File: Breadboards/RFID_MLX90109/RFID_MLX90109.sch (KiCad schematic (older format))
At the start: 24 parts, among them P101 CONN_01X08, Q101 Q_NMOS_GSD, U101 MLX90109

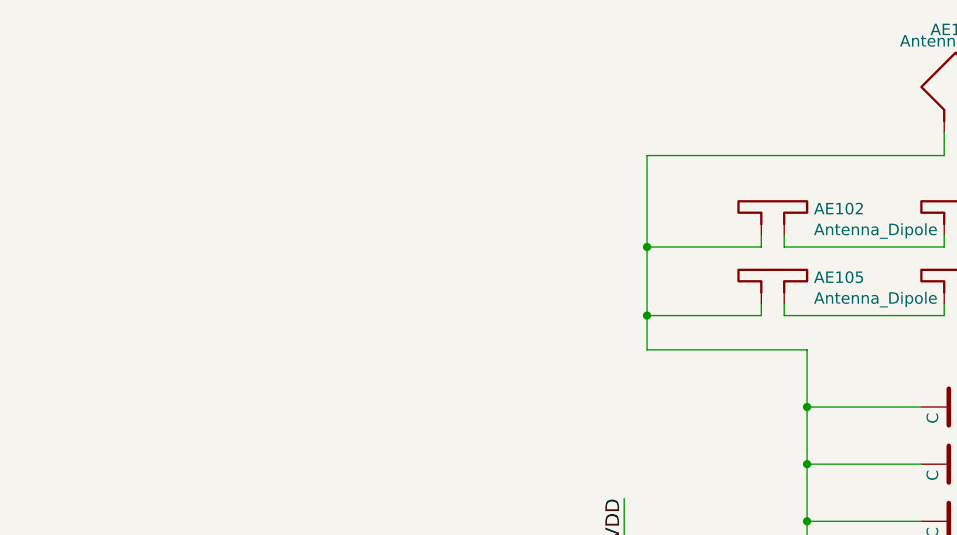
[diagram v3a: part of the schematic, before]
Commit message: Adds 2 Antennas for 125kHz antenna (Back and Front)
- Antenna is connected via 2 jumpers
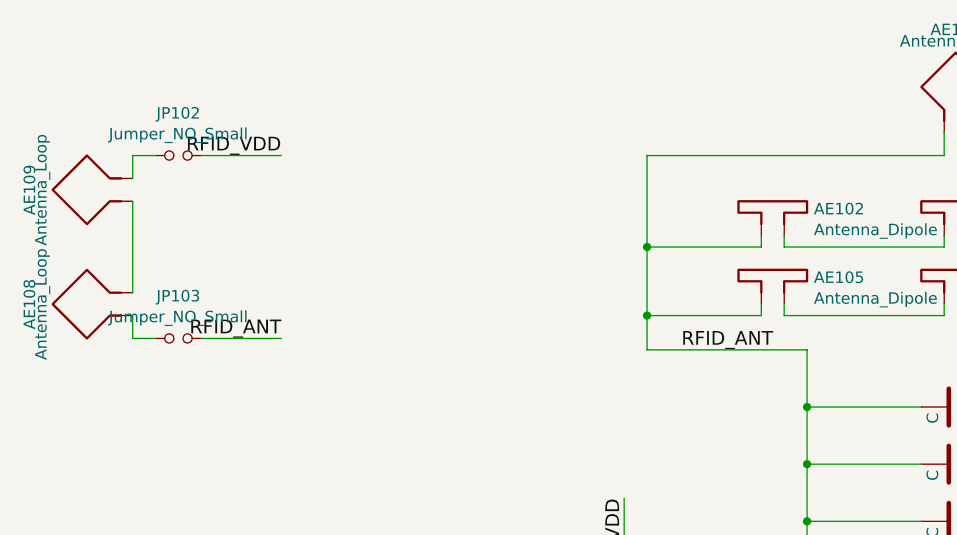
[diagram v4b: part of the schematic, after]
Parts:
- added AE108, AE109: Antenna_Loop, Octanis3:125kHz_PCB_Antenna, symbol Antenna_Loop
- added JP102, JP103: Jumper_NO_Small, Pin_Headers:Pin_Header_Straight_1x02_Pitch2.54mm, symbol Jumper_NO_Small
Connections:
- net labels added: RFID_ANT
- wire segments 75 -> 82
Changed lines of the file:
@@
 	1    0    0    -1
 $EndComp
-Wire Wire Line
-	5850 3200 6950 3200
-Wire Wire Line
-	5800 3650 7550 3650
-Wire Wire Line
-	5800 3800 7550 3800
-Wire Wire Line
-	4200 3650 4800 3650
-Wire Wire Line
-	4250 3950 4800 3950
-Connection ~ 4500 3950
-Wire Wire Line
-	3250 3950 3950 3950
-Wire Wire Line
-	3700 3800 4800 3800
-Wire Wire Line
-	4600 3500 4800 3500
-Wire Wire Line
-	4600 3050 5100 3050
-Wire Wire Line
-	5850 3050 5400 3050
-Wire Wire Line
-	5850 2050 5850 3500
-Connection ~ 5850 3200
-Connection ~ 4600 3050
-Connection ~ 5850 3050
-Wire Wire Line
-	4500 3950 4500 4400
-Wire Wire Line
-	3950 4200 3800 4200
-Wire Wire Line
-	3800 4200 3800 3950
-Connection ~ 3800 3950
-Wire Wire Line
-	4500 4200 4250 4200
-Connection ~ 4500 4200
-Connection ~ 4300 3650
-Connection ~ 4700 3950
-Wire Wire Line
-	4500 4700 4500 4800
-Wire Wire Line
-	4600 2800 5100 2800
-Connection ~ 4600 2800
-Connection ~ 4600 2550
-Wire Wire Line
-	4600 2050 4600 3500
-Wire Wire Line
-	4600 2550 5100 2550
-Wire Wire Line
-	5400 2550 5850 2550
-Connection ~ 5850 2550
-Wire Wire Line
-	5400 2800 5850 2800
-Connection ~ 5850 2800
-Wire Wire Line
-	4600 2300 5100 2300
-Connection ~ 4600 2300
-Wire Wire Line
-	5400 2300 5850 2300
-Connection ~ 5850 2300
-Wire Wire Line
-	8950 2550 8950 3050
-Wire Wire Line
-	3800 3100 3800 2700
-Wire Wire Line
-	3800 3400 3800 3800
-Connection ~ 3800 3800
-Wire Wire Line
-	3400 3800 3350 3800
-Wire Wire Line
-	5800 3950 6100 3950
-Wire Wire Line
-	6000 3950 6000 4250
-Connection ~ 6000 3950
-Wire Wire Line
-	6400 3950 6900 3950
-Wire Wire Line
-	4500 5200 4500 5300
-Wire Wire Line
-	4100 5000 4200 5000
-Wire Wire Line
-	5850 3500 5800 3500
-Wire Wire Line
-	6650 3600 6650 3800
-Connection ~ 6650 3800
-Wire Wire Line
-	6650 3200 6650 3300
-Connection ~ 6650 3200
-Wire Wire Line
-	6950 3600 6950 3650
-Connection ~ 6950 3650
-Wire Wire Line
-	6950 3200 6950 3300
-Wire Wire Line
-	5300 1550 5300 1600
-Wire Wire Line
-	5300 1600 6000 1600
-Wire Wire Line
-	6000 1600 6000 1550
-Wire Wire Line
-	4500 1850 4500 1900
-Wire Wire Line
-	4500 1900 5200 1900
-Wire Wire Line
-	5200 1900 5200 1850
-Wire Wire Line
-	5300 1850 5300 1900
-Wire Wire Line
-	5300 1900 6000 1900
-Wire Wire Line
-	6000 1900 6000 1850
-Wire Wire Line
-	4500 1550 4500 1600
-Wire Wire Line
-	4500 1600 5200 1600
-Wire Wire Line
-	5200 1600 5200 1550
-Wire Wire Line
-	3900 1200 3900 2050
-Wire Wire Line
-	3900 2050 4600 2050
-Wire Wire Line
-	5200 1100 5200 1200
-Wire Wire Line
-	5200 1200 3900 1200
-Wire Wire Line
-	5300 1100 5300 1200
-Wire Wire Line
-	5300 1200 6850 1200
-Wire Wire Line
-	6850 1200 6850 2050
-Wire Wire Line
-	6850 2050 5850 2050
-Wire Wire Line
-	6100 1550 6100 1600
-Wire Wire Line
-	6100 1600 6850 1600
-Connection ~ 6850 1600
-Wire Wire Line
-	6100 1850 6100 1900
-Wire Wire Line
-	6100 1900 6850 1900
-Connection ~ 6850 1900
-Wire Wire Line
-	4400 1550 4400 1600
-Wire Wire Line
-	4400 1600 3900 1600
-Connection ~ 3900 1600
-Wire Wire Line
-	4400 1850 4400 1900
-Wire Wire Line
-	4400 1900 3900 1900
-Connection ~ 3900 1900
-Wire Wire Line
-	3800 3500 3250 3500
-Connection ~ 3800 3500
 Text Label 3250 3500 0    60   ~ 0
 RFID_SPEED
@@
 Text Label 7100 3800 0    60   ~ 0
 RFID_CLOCK
-Wire Wire Line
-	6000 4150 6900 4150
-Connection ~ 6000 4150
 Text Label 6450 4150 0    60   ~ 0
 RFID_MODE
-Wire Wire Line
-	10350 3500 9700 3500
-Wire Wire Line
-	10350 3600 9700 3600
-Wire Wire Line
-	10350 3700 9700 3700
-Wire Wire Line
-	10350 3800 9700 3800
-Wire Wire Line
-	10350 3900 9700 3900
-Wire Wire Line
-	10350 4000 9700 4000
 Text Label 9700 3800 0    60   ~ 0
 RFID_CLOCK
@@
 	1    0    0    -1
 $EndComp
-Wire Wire Line
-	10350 4100 9700 4100
-Wire Wire Line
-	10350 4200 9700 4200
 Text Label 9700 4100 0    60   ~ 0
 RFID_SPEED
@@
 	1    0    0    -1
 $EndComp
+$Comp
+L Antenna_Loop AE108
+U 1 1 5A1309D1
+P 1450 1900
+F 0 "AE108" H 1500 2150 50  0000 C CNN
+F 1 "Antenna_Loop" H 1500 2100 50  0000 C CNN
+F 2 "Octanis3:125kHz_PCB_Antenna" H 1450 1900 50  0001 C CNN
+F 3 "" H 1450 1900 50  0001 C CNN
+	1    1450 1900
+	0    -1   -1   0
+$EndComp
+$Comp
+L Antenna_Loop AE109
+U 1 1 5A130BD8
+P 1450 1300
+F 0 "AE109" H 1500 1550 50  0000 C CNN
+F 1 "Antenna_Loop" H 1500 1500 50  0000 C CNN
+F 2 "Octanis3:125kHz_PCB_Antenna" H 1450 1300 50  0001 C CNN
+F 3 "" H 1450 1300 50  0001 C CNN
+	1    1450 1300
+	0    -1   1    0
+$EndComp
+$Comp
+L Jumper_NO_Small JP102
+U 1 1 5A130D13
+P 1850 1200
+F 0 "JP102" H 1850 1385 50  0000 C CNN
+F 1 "Jumper_NO_Small" H 1850 1294 50  0000 C CNN
+F 2 "Pin_Headers:Pin_Header_Straight_1x02_Pitch2.54mm" H 1850 1200 50  0001 C CNN
+F 3 "" H 1850 1200 50  0000 C CNN
+	1    1850 1200
+	1    0    0    -1
+$EndComp
+$Comp
+L Jumper_NO_Small JP103
+U 1 1 5A131038
+P 1850 2000
+F 0 "JP103" H 1850 2185 50  0000 C CNN
+F 1 "Jumper_NO_Small" H 1850 2094 50  0000 C CNN
+F 2 "Pin_Headers:Pin_Header_Straight_1x02_Pitch2.54mm" H 1850 2000 50  0001 C CNN
+F 3 "" H 1850 2000 50  0000 C CNN
+	1    1850 2000
+	1    0    0    -1
+$EndComp
+Wire Wire Line
+	5850 3200 6950 3200
+Wire Wire Line
+	5800 3650 7550 3650
+Wire Wire Line
+	5800 3800 7550 3800
+Wire Wire Line
+	4200 3650 4800 3650
+Wire Wire Line
+	4250 3950 4800 3950
+Connection ~ 4500 3950
+Wire Wire Line
+	3250 3950 3950 3950
+Wire Wire Line
+	3700 3800 4800 3800
+Wire Wire Line
+	4600 3500 4800 3500
+Wire Wire Line
+	4600 3050 5100 3050
+Wire Wire Line
+	5850 3050 5400 3050
+Wire Wire Line
+	5850 2050 5850 3500
+Connection ~ 5850 3200
+Connection ~ 4600 3050
+Connection ~ 5850 3050
+Wire Wire Line
+	4500 3950 4500 4400
+Wire Wire Line
+	3950 4200 3800 4200
+Wire Wire Line
+	3800 4200 3800 3950
+Connection ~ 3800 3950
+Wire Wire Line
+	4500 4200 4250 4200
+Connection ~ 4500 4200
+Connection ~ 4300 3650
+Connection ~ 4700 3950
+Wire Wire Line
+	4500 4700 4500 4800
+Wire Wire Line
+	4600 2800 5100 2800
+Connection ~ 4600 2800
+Connection ~ 4600 2550
+Wire Wire Line
+	4600 2050 4600 3500
+Wire Wire Line
+	4600 2550 5100 2550
+Wire Wire Line
+	5400 2550 5850 2550
+Connection ~ 5850 2550
+Wire Wire Line
+	5400 2800 5850 2800
+Connection ~ 5850 2800
+Wire Wire Line
+	4600 2300 5100 2300
+Connection ~ 4600 2300
+Wire Wire Line
+	5400 2300 5850 2300
+Connection ~ 5850 2300
+Wire Wire Line
+	8950 2550 8950 3050
+Wire Wire Line
+	3800 3100 3800 2700
+Wire Wire Line
+	3800 3400 3800 3800
+Connection ~ 3800 3800
+Wire Wire Line
+	3400 3800 3350 3800
+Wire Wire Line
+	5800 3950 6100 3950
+Wire Wire Line
+	6000 3950 6000 4250
+Connection ~ 6000 3950
+Wire Wire Line
+	6400 3950 6900 3950
+Wire Wire Line
+	4500 5200 4500 5300
+Wire Wire Line
+	4100 5000 4200 5000
+Wire Wire Line
+	5850 3500 5800 3500
+Wire Wire Line
+	6650 3600 6650 3800
+Connection ~ 6650 3800
+Wire Wire Line
+	6650 3200 6650 3300
+Connection ~ 6650 3200
+Wire Wire Line
+	6950 3600 6950 3650
+Connection ~ 6950 3650
+Wire Wire Line
+	6950 3200 6950 3300
+Wire Wire Line
+	5300 1550 5300 1600
+Wire Wire Line
+	5300 1600 6000 1600
+Wire Wire Line
+	6000 1600 6000 1550
+Wire Wire Line
+	4500 1850 4500 1900
+Wire Wire Line
+	4500 1900 5200 1900
+Wire Wire Line
+	5200 1900 5200 1850
+Wire Wire Line
+	5300 1850 5300 1900
+Wire Wire Line
+	5300 1900 6000 1900
+Wire Wire Line
+	6000 1900 6000 1850
+Wire Wire Line
+	4500 1550 4500 1600
+Wire Wire Line
+	4500 1600 5200 1600
+Wire Wire Line
+	5200 1600 5200 1550
+Wire Wire Line
+	3900 1200 3900 2050
+Wire Wire Line
+	3900 2050 4600 2050
+Wire Wire Line
+	5200 1100 5200 1200
+Wire Wire Line
+	5200 1200 3900 1200
+Wire Wire Line
+	5300 1100 5300 1200
+Wire Wire Line
+	5300 1200 6850 1200
+Wire Wire Line
+	6850 1200 6850 2050
+Wire Wire Line
+	6850 2050 5850 2050
+Wire Wire Line
+	6100 1550 6100 1600
+Wire Wire Line
+	6100 1600 6850 1600
+Connection ~ 6850 1600
+Wire Wire Line
+	6100 1850 6100 1900
+Wire Wire Line
+	6100 1900 6850 1900
+Connection ~ 6850 1900
+Wire Wire Line
+	4400 1550 4400 1600
+Wire Wire Line
+	4400 1600 3900 1600
+Connection ~ 3900 1600
+Wire Wire Line
+	4400 1850 4400 1900
+Wire Wire Line
+	4400 1900 3900 1900
+Connection ~ 3900 1900
+Wire Wire Line
+	3800 3500 3250 3500
+Connection ~ 3800 3500
+Wire Wire Line
+	6000 4150 6900 4150
+Connection ~ 6000 4150
+Wire Wire Line
+	10350 3500 9700 3500
+Wire Wire Line
+	10350 3600 9700 3600
+Wire Wire Line
+	10350 3700 9700 3700
+Wire Wire Line
+	10350 3800 9700 3800
+Wire Wire Line
+	10350 3900 9700 3900
+Wire Wire Line
+	10350 4000 9700 4000
+Wire Wire Line
+	10350 4100 9700 4100
+Wire Wire Line
+	10350 4200 9700 4200
+Wire Wire Line
+	1650 1900 1650 2000
+Wire Wire Line
+	1650 2000 1750 2000
+Wire Wire Line
+	1650 1800 1650 1400
+Wire Wire Line
+	1650 1300 1650 1200
+Wire Wire Line
+	1650 1200 1750 1200
+Wire Wire Line
+	1950 1200 2300 1200
+Wire Wire Line
+	1950 2000 2300 2000
+Text Label 2300 1200 2    60   ~ 0
+RFID_VDD
+Text Label 4050 2050 0    60   ~ 0
+RFID_ANT
+Text Label 2300 2000 2    60   ~ 0
+RFID_ANT
 $EndSCHEMATC

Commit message: new LF antenna plus diverse comments;
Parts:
- R102, R103: value R -> 100k
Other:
- note added: "recommended: 100k values for power savings,\nMSP430 internal pull-ups are 35k (20-50k)"
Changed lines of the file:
@@
 LIBS:transistors
 LIBS:conn
+LIBS:linear
 LIBS:regul
 LIBS:74xx
@@
 P 6650 3450
 F 0 "R102" H 6720 3496 50  0000 L CNN
-F 1 "R" H 6720 3405 50  0000 L CNN
+F 1 "100k" H 6720 3405 50  0000 L CNN
 F 2 "Resistors_SMD:R_0603_HandSoldering" V 6580 3450 50  0001 C CNN
 F 3 "" H 6650 3450 50  0001 C CNN
@@
 P 6950 3450
 F 0 "R103" H 7020 3496 50  0000 L CNN
-F 1 "R" H 7020 3405 50  0000 L CNN
+F 1 "100k" H 7020 3405 50  0000 L CNN
 F 2 "Resistors_SMD:R_0603_HandSoldering" V 6880 3450 50  0001 C CNN
 F 3 "" H 6950 3450 50  0001 C CNN
@@
 Text Label 2300 2000 2    60   ~ 0
 RFID_ANT
+Text Notes 6300 3050 0    60   ~ 0
+recommended: 100k values for power savings,\nMSP430 internal pull-ups are 35k (20-50k)
 $EndSCHEMATC
